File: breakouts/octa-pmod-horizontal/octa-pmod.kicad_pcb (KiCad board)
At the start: 2 copper layers, 89 x 63.8 mm, 21 parts, among them J1 PMOD, J10 PMOD, J11 PWR, J12 PWR, J13 PWR, J14 PWR, J15 PMOD, J16 PMOD, J2 PMOD, J3 S7 Mini, J4 S7 Mini, J5 PWR, J6 PWR, J7 PMOD, J8 PMOD, J9 PMOD, M1 M3, M2 M3, M3 M3, M4 M3

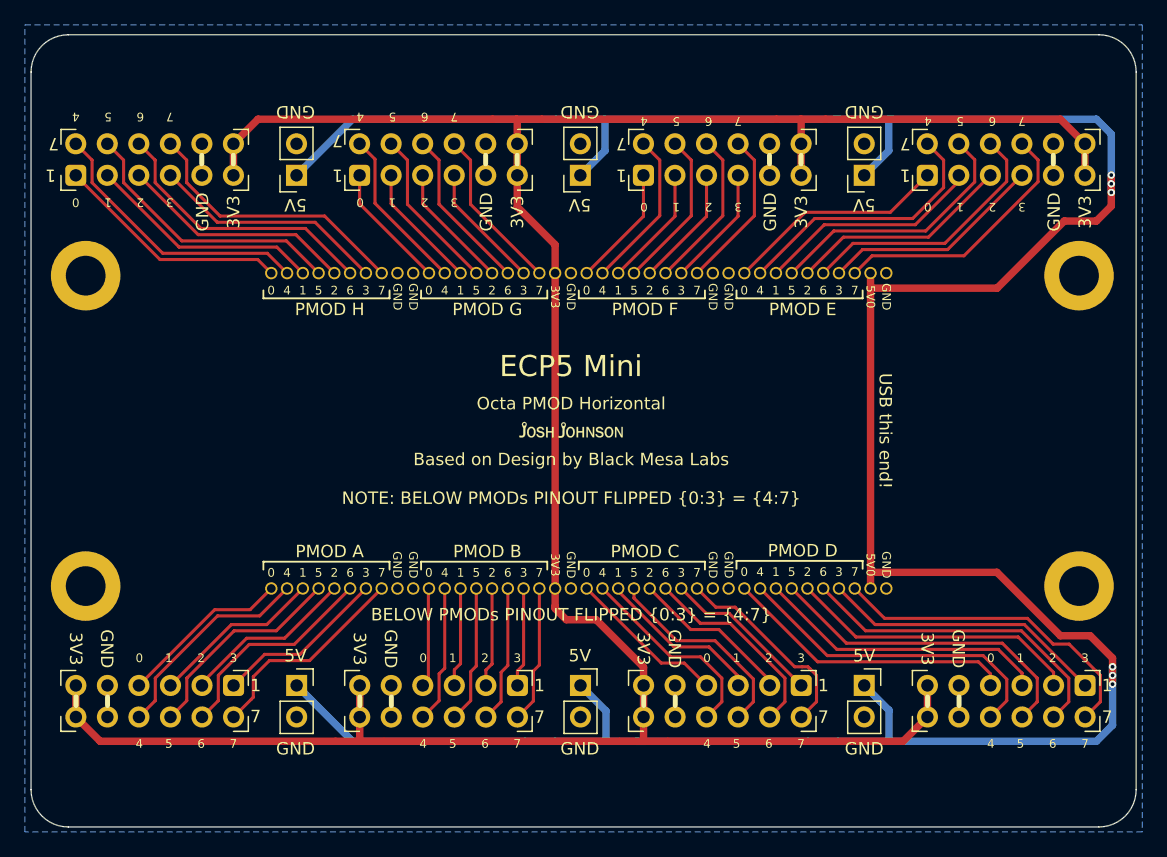
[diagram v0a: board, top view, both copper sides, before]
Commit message: update silk to clear connectors
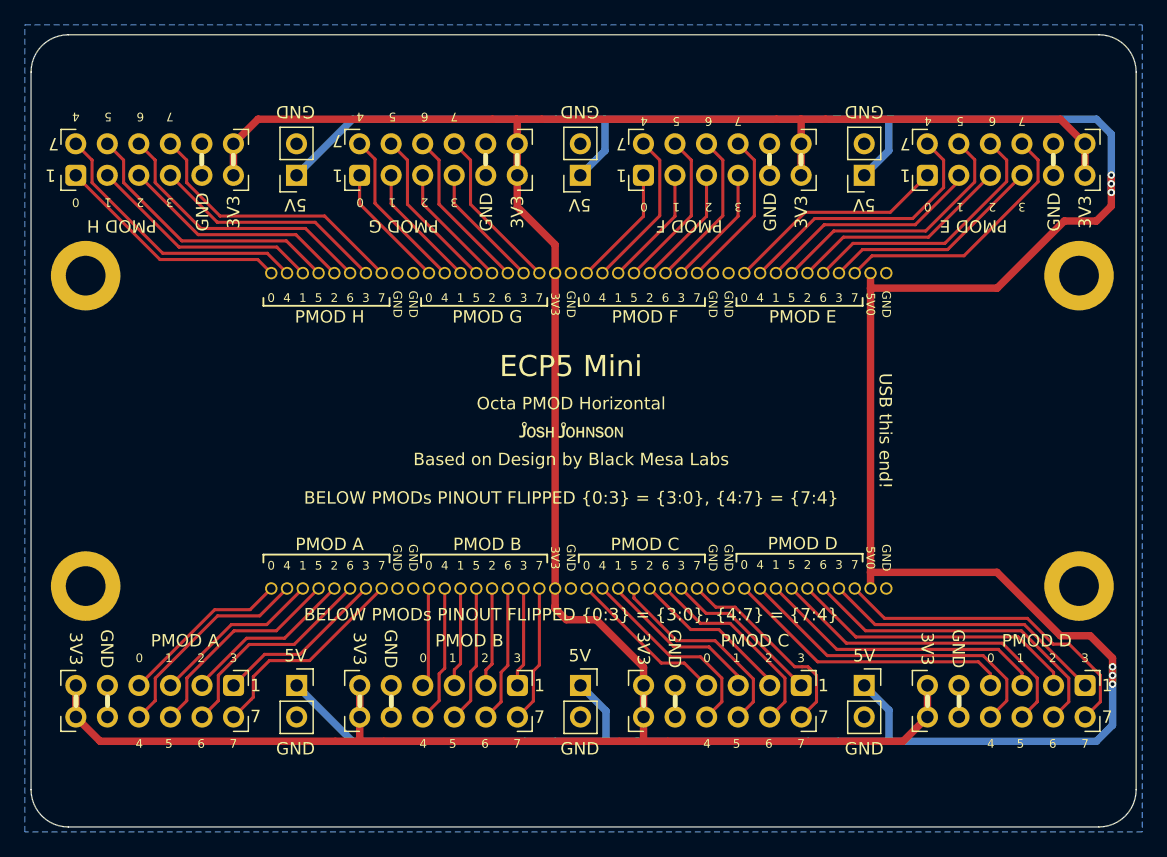
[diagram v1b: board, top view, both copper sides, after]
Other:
- board text added: "BELOW PMODs PINOUT FLIPPED {0:3} = {3:0}, {4:7} = {7:4}"
- board text removed: "BELOW PMODs PINOUT FLIPPED {0:3} = {4:7}"
- board text removed: "NOTE: BELOW PMODs PINOUT FLIPPED {0:3} = {4:7}"
